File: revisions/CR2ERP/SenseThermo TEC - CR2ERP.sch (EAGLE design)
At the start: 61 parts, among them Q1 mmbt2222, Q3 6.5A/30V/38mΩ, U1 MIC5225-3.3, U2 AT21CS01, U3 MAX31865, U4 MAX31865, U5 MAX31865, U6 MAX31865, U8 VNH5019

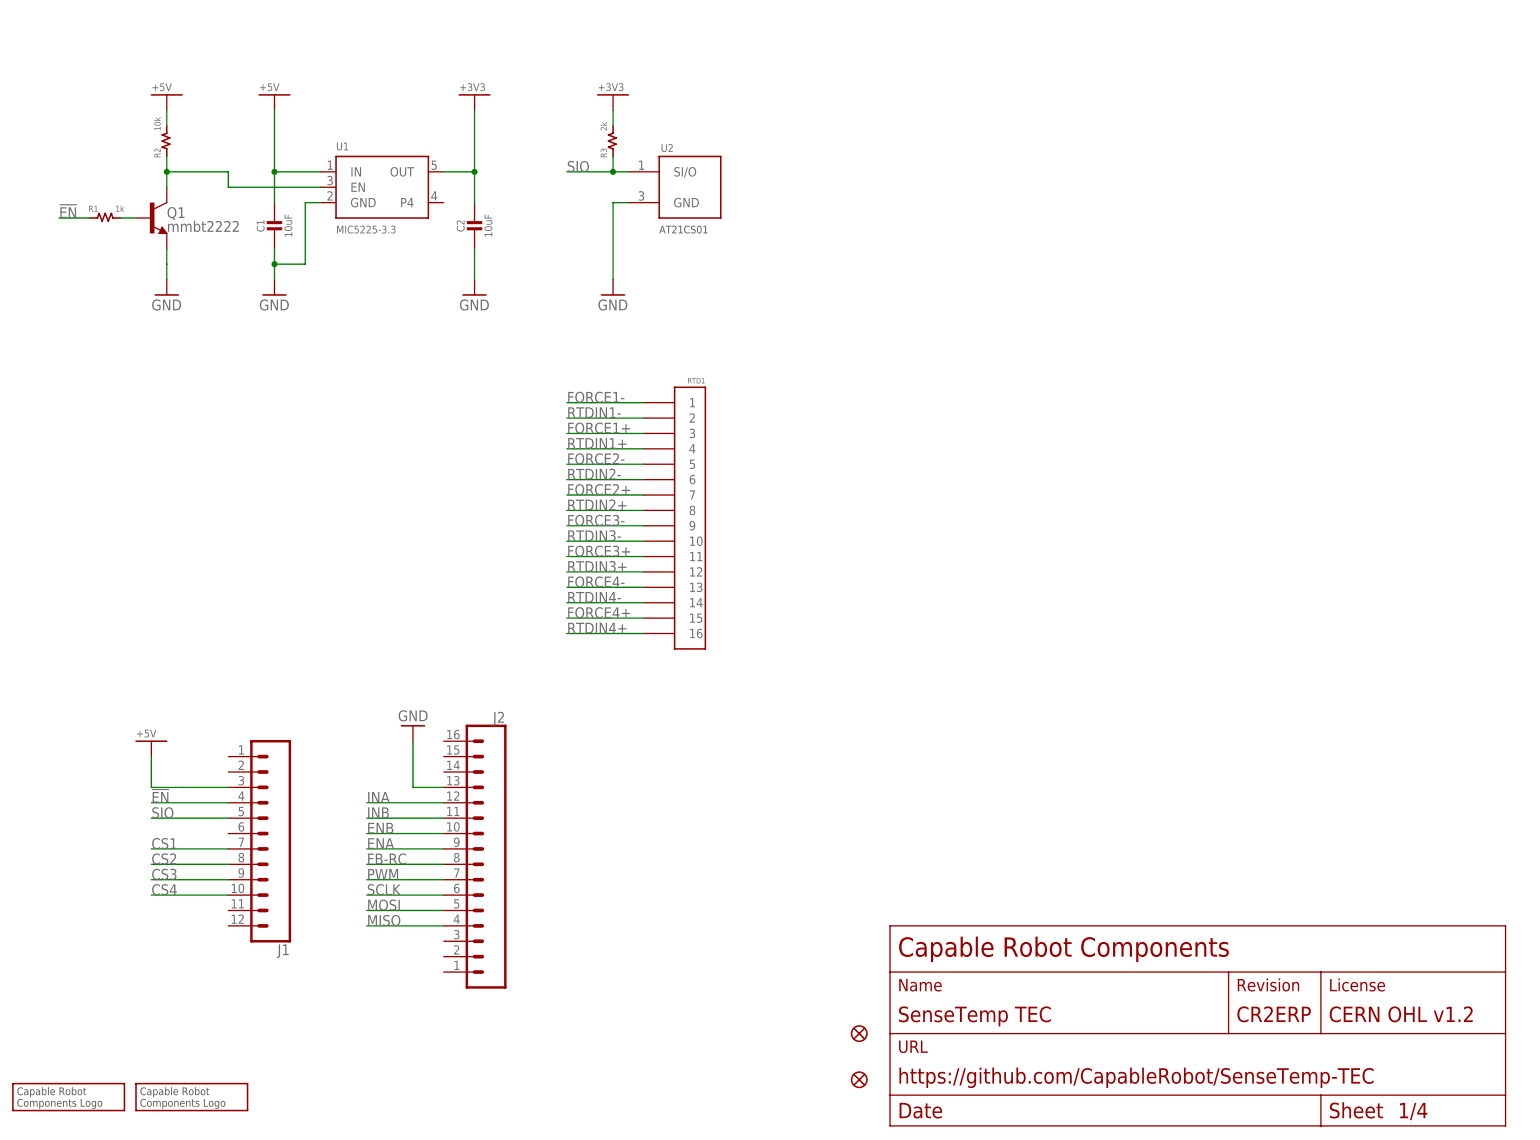
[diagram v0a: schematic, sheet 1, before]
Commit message: Remove 5v to 3v regulator (will be replaced by 12v to 3v regulator.  Change TEC PWM pin.
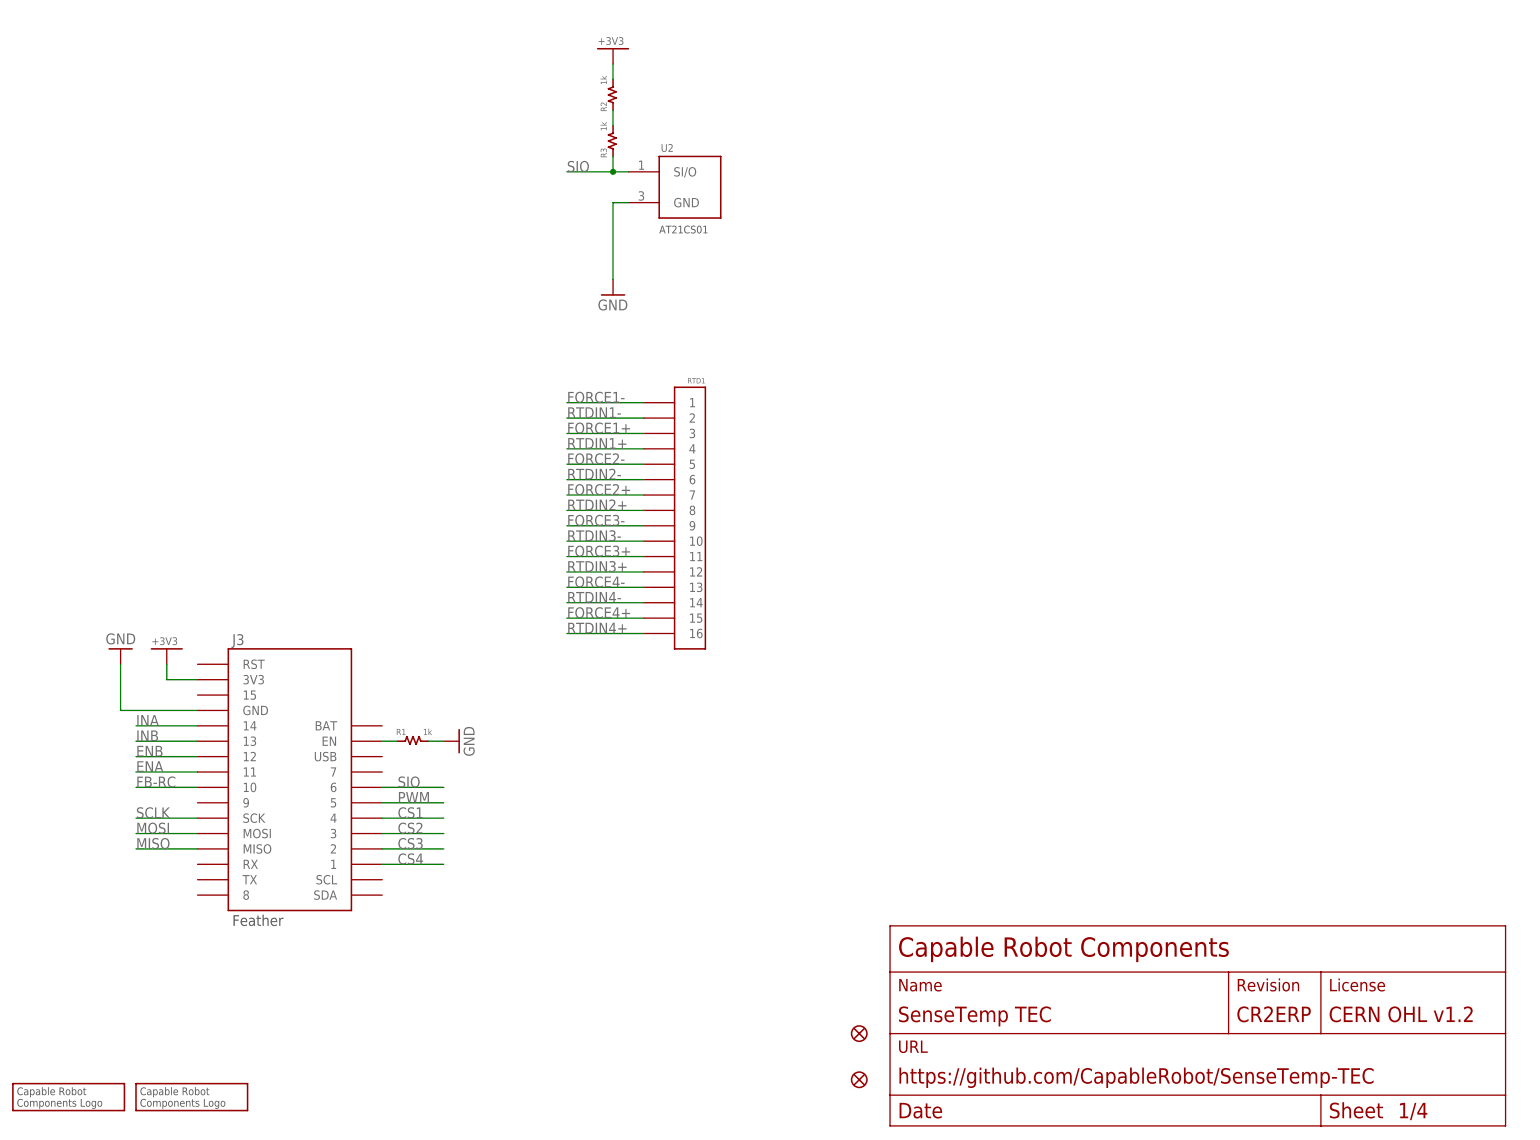
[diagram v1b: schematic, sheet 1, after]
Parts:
- removed C1, C2: 10uF, microbuilder:CAP_CERAMIC1206
- removed J1: (no value), SparkFun-Connectors:CONN_12NO_SILK
- removed J2: (no value), SparkFun-Connectors:CONN_161X16_NO_SILK
- removed Q1: mmbt2222, SparkFun-DiscreteSemi:TRANS_NPN-MMBT2222AL
- removed U1: MIC5225-3.3, microbuilder:VREG_SOT23-5
- added J3: FEATHERPTH, CapableRobot:FEATHERPTH
- R2: value 10k -> 1k
- R3: value 2k -> 1k
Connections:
- removed net !EN: J1.4, R1.1
- removed net +5V: C1.P$1, J1.3, R2.2, U1.IN
- removed net N$3: Q1.C, R2.1, U1.EN
- new net EN: J3.EN, R1.1
- net +3V3: now also J3.3V3, R2.2; no longer C2.P$1, R3.2, U1.OUT
- net CS1: now also J3.4; no longer J1.7
- net CS2: now also J3.3; no longer J1.8
- net CS3: now also J3.2; no longer J1.9
- net CS4: now also J3.1; no longer J1.10
- net ENA: now also J3.11; no longer J2.9
- net ENB: now also J3.12; no longer J2.10
- net FB-RC: now also J3.10; no longer J2.8
- net GND: now also J3.GND, R1.2; no longer C1.P$2, C2.P$2, J2.13, Q1.E, U1.GND
- net INA: now also J3.14; no longer J2.12
- net INB: now also J3.13; no longer J2.11
- net MISO: now also J3.MISO; no longer J2.4
- net MOSI: now also J3.MOSI; no longer J2.5
- net N$4: now also R2.1, R3.2; no longer Q1.B, R1.2
- net PWM: now also J3.5; no longer J2.7
- net SCLK: now also J3.SCK; no longer J2.6
- net SIO: now also J3.6; no longer J1.5
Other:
- moved on the sheet: R1, R2

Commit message: Added 12v to 5v regulator and 5v to 3v regulators.  Changed RTD passives to 0603
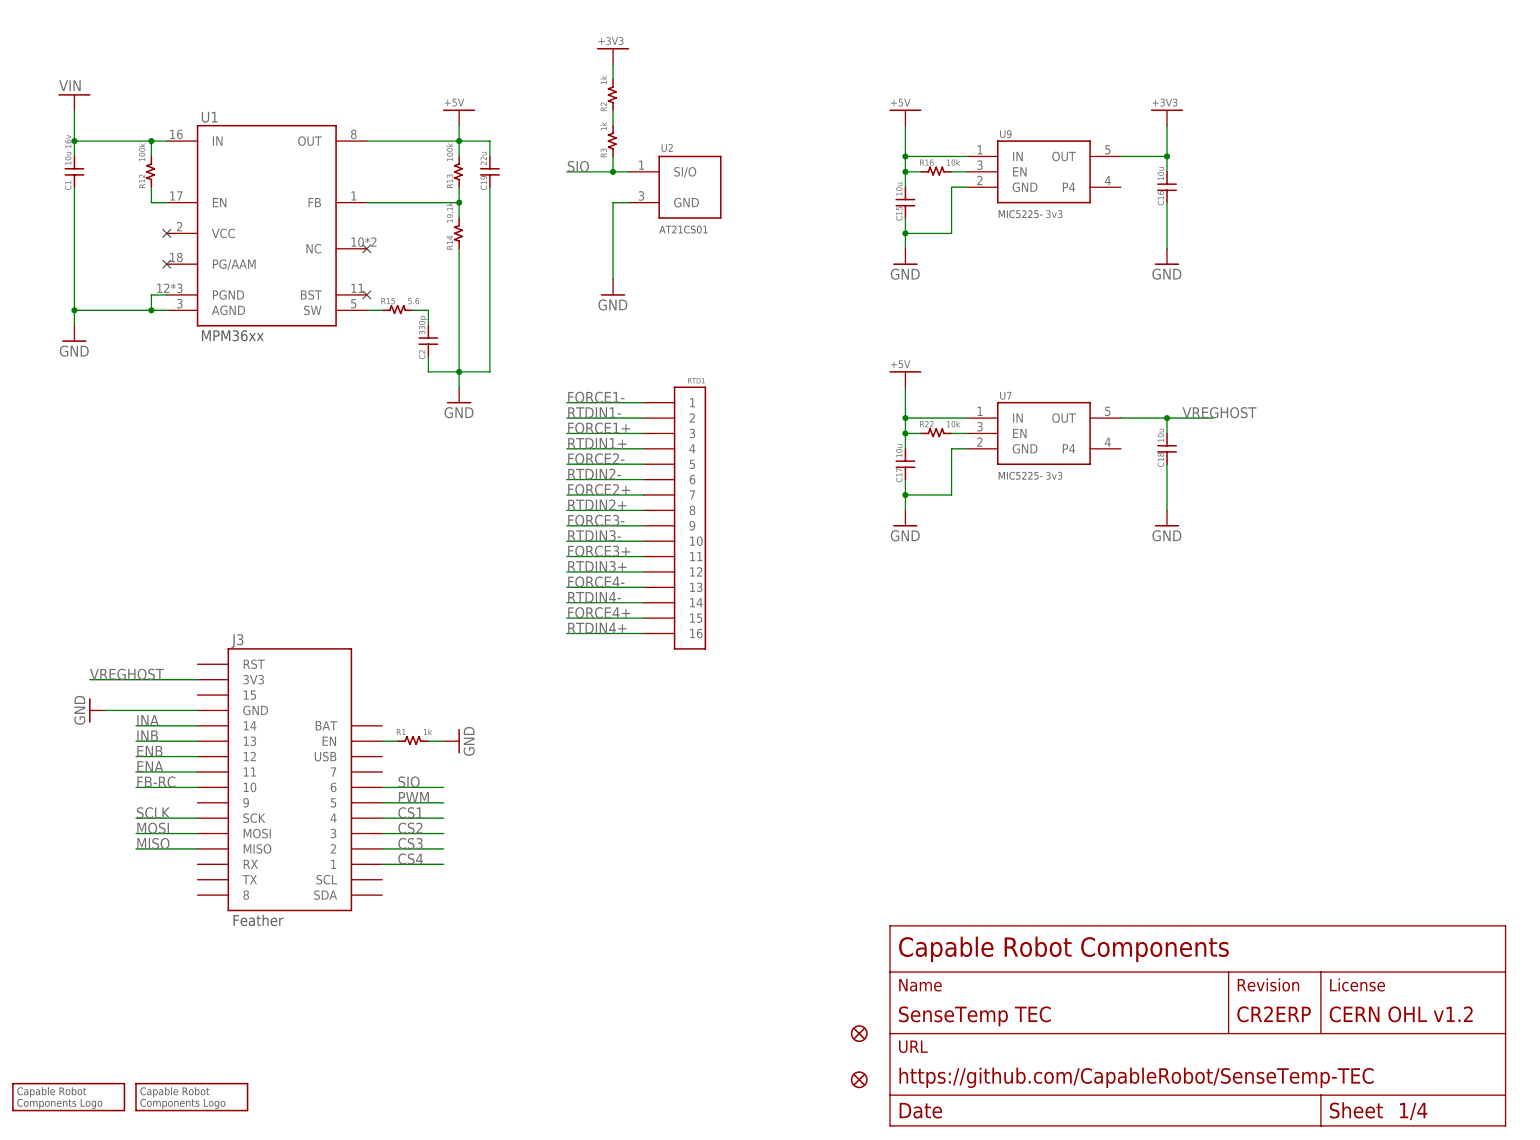
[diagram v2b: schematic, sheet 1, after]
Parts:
- removed C24: (no value), CapableRobot:CAP1206
- added C1: 10u 16v, CapableRobot:CAP1206
- added C15, C16, C17, C18: 10u, CapableRobot:CAP0805
- added C19: 22u, CapableRobot:CAP0805
- added C2: 330p, CapableRobot:CAP0603
- added R12, R13: 100k, CapableRobot:RES0603
- added R14: 19.1k, CapableRobot:RES0603
- added R15: 5.6, CapableRobot:RES0603
- added R16, R22: 10k, CapableRobot:RES0603
- added U1: (no value), CapableRobot:MPM36XX
- added U7, U9: 3v3, CapableRobot:MIC5225
- C10, C12, C13, C3, C4, C6, C7, C9: value 0.1uF -> 100n; device microbuilder:CAP_CERAMIC_0805MP -> CapableRobot:CAP0603
- C11, C14, C5, C8: value 10nF -> 10n; device microbuilder:CAP_CERAMIC_0805MP -> CapableRobot:CAP0603
- FB1, FB2, FB3, FB4: device microbuilder:FERRITE_0805MP -> CapableRobot:FER0603
- LOGO1: value CRC-LOGO10 -> CRC-LOGO7; device CapableRobot:CRC-LOGO10 -> CapableRobot:CRC-LOGO7
- R11, R5, R7, R9: value 4300Ω 0.1% -> 4k3 0.1%; device microbuilder:RESISTOR_0805MP -> CapableRobot:RES0603
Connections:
- new net +5V: C15.P$2, C17.P$2, C19.P$2, R13.2, R16.1, R22.1, U1.OUT, U7.IN, U9.IN
- new net FBMPM: R13.1, R14.2, U1.FB
- new net N$18: C2.P$2, R15.2
- new net N$20: R16.2, U9.EN
- new net N$23: R22.2, U7.EN
- new net N$3: R12.1, U1.EN
- new net SNUB: R15.1, U1.SW
- new net VREGHOST: C18.P$2, J3.3V3, R20.2, R21.2, U7.OUT
- net +3V3: now also C16.P$2, U9.OUT; no longer J3.3V3, R20.2, R21.2
- net GND: now also C1.P$1, C15.P$1, C16.P$1, C17.P$1, C18.P$1, C19.P$1, C2.P$1, R14.1, U1.AGND, U1.PGND, U7.GND, U9.GND; no longer C24.P$1
- net VIN: now also C1.P$2, R12.2, U1.IN; no longer C24.P$2
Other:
- note added: "Connected to this net instead of 3V3 to simply routing"
- moved on the sheet: C10, C11, C12, C13, C14, C3, C4, C5, C6, C7, C8, C9

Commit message: Added high side switch for fan.  Silkscreen changes.
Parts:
- removed TEC: CONN-2-MFJR-RA, CapableRobot:CONN-2-MFJR-RA
- added C24, C25: 22u 16v, CapableRobot:CAP1206
- added R23: 10k, CapableRobot:RES0603
- added TEC/FAN: CONN-4-MFJR-RA, CapableRobot:CONN-4-MFJR-RA
- added U10: NCV8461, CapableRobot:NCV8461
- Q3: device SparkFun-DiscreteSemi:MOSFET-NCH-FDS6630A -> CapableRobot:MOSFET-NCH-SOIC8
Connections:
- new net AGND: R14.1, U1.AGND
- new net FANCTRL: J3.TX, R23.2, U10.IN
- new net FANPWR: C24.P$2, C25.P$2, TEC/FAN.2, U10.OUT
- new net FANSTAT: J3.RX, U10.STAT
- net GND: now also C24.P$1, C25.P$1, R23.1, TEC/FAN.4, U10.GND; no longer R14.1, U1.AGND
- net TECM: now also TEC/FAN.3; no longer TEC.2
- net TECP: now also TEC/FAN.1; no longer TEC.1
- net VIN: now also U10.VDD

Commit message: Update to released version of CR2ERP
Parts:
- removed C17, C18: 10u, CapableRobot:CAP0805
- removed C2: 330p, CapableRobot:CAP0603
- removed R1: 1k, CapableRobot:RES0603
- removed R12, R13: 100k, CapableRobot:RES0603
- removed R14: 19.1k, CapableRobot:RES0603
- removed R15: 5.6, CapableRobot:RES0603
- removed R22: 10k, CapableRobot:RES0603
- removed U9: 3v3, CapableRobot:MIC5225
- added C26: 10u, CapableRobot:CAP0805
- added D1: MBR120, Adafruit Feather M0 Express:DIODE-SCHOTTKYSOD-123
- C1: value 10u 16v -> 22u 16v
- C19: value 22u -> 10u
- C20: value (none) -> 100n
- C22, C23: value (none) -> 22u 16v
- D3: value SM6J12A -> SMAJ12A; MPN (none) -> SMAJ12A-13-F
- D4: MPN (none) -> SMAJ12A-13-F
- FB1, FB2, FB3, FB4: value (none) -> 600R
- LOGO1: value CRC-LOGO7 -> CRC-LOGO7SILK; device CapableRobot:CRC-LOGO7 -> CapableRobot:CRC-LOGO7SILK
- Q3: MPN (none) -> FDS6630A
- R11, R5, R7, R9: value 4k3 0.1% -> 4k3 0.05%
- R17, R19: value 10K -> 10k
- R18: value 1K -> 1k
- RTD1: MPN (none) -> 3221-16-0300-00
- U1: value (none) -> NCP1117 3v3; device CapableRobot:MPM36XX -> CapableRobot:VREG-LDO; MPN (none) -> NCP1117ST50T3G
- U10: MPN (none) -> NCV8461DR2G
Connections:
- removed net AGND: R14.1, U1.AGND
- removed net EN: J3.EN, R1.1
- removed net FBMPM: R13.1, R14.2, U1.FB
- removed net N$18: C2.P$2, R15.2
- removed net N$23: R22.2, U7.EN
- removed net N$3: R12.1, U1.EN
- removed net SNUB: R15.1, U1.SW
- new net VHOST: D1.C, J3.USB
- net +3V3: now also U7.OUT; no longer U9.OUT
- net +5V: now also C26.P$2, D1.A, U1.VOUT; no longer C17.P$2, R13.2, R22.1, U1.OUT, U9.IN
- net GND: now also C26.P$1, U1.GND; no longer C17.P$1, C18.P$1, C2.P$1, R1.2, U1.PGND, U9.GND
- net N$20: now also U7.EN; no longer U9.EN
- net VIN: now also U1.VIN; no longer R12.2, U1.IN
- net VREGHOST: no longer C18.P$2, U7.OUT
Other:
- note added: "Connected to this net instead of 3V3 to simplify routing"
- note removed: "Connected to this net instead of 3V3 to simply routing"
- moved on the sheet: C19, U7
